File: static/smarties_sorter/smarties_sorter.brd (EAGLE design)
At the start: 170.2 x 100 mm, 18 parts, among them IC1 MEGA8-P, Q1 16Mhz, Q2 IRLZ44Z

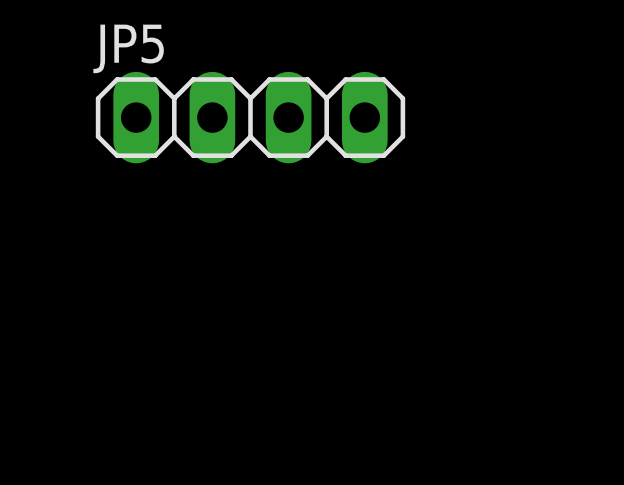
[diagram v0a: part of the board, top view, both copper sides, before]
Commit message: [smarties_sorter] Adds capa on the motor
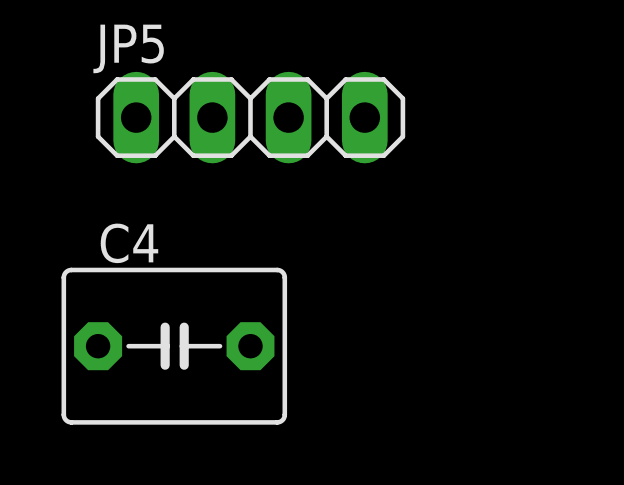
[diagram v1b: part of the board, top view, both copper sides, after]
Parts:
- added C4: 10µF, capacitor-wima:C5B5
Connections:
- net 5V: now also C4.2
- net N$7: now also C4.1
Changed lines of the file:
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@@
 <element name="R1" library="rcl" package="0414/15" value="10Kohms" x="8.89" y="-5.08"/>
 <element name="JP5" library="pinhead" package="1X04" value="" x="6.35" y="-11.43"/>
+<element name="C4" library="capacitor-wima" package="C5B5" value="10µF" x="3.81" y="-19.05"/>
 </elements>
 <signals>
@@
 <wire x1="57.15" y1="67.31" x2="60.96" y2="67.31" width="0.8128" layer="16"/>
 <contactref element="JP5" pad="1"/>
+<contactref element="C4" pad="2"/>
 <wire x1="110.49" y1="67.31" x2="102.87" y2="67.31" width="0" layer="19" extent="16-16"/>
 <wire x1="2.54" y1="-11.43" x2="52.07" y2="31.75" width="0" layer="19" extent="16-16"/>
+<wire x1="6.35" y1="-19.05" x2="2.54" y2="-11.43" width="0" layer="19" extent="1-1"/>
 </signal>
 <signal name="N$6">
@@
 <wire x1="49.53" y1="64.77" x2="48.26" y2="64.77" width="0.8128" layer="16"/>
 <contactref element="D2" pad="A"/>
+<contactref element="C4" pad="1"/>
+<wire x1="1.27" y1="-19.05" x2="48.26" y2="64.77" width="0" layer="19" extent="1-1"/>
 </signal>
 <signal name="N$9">

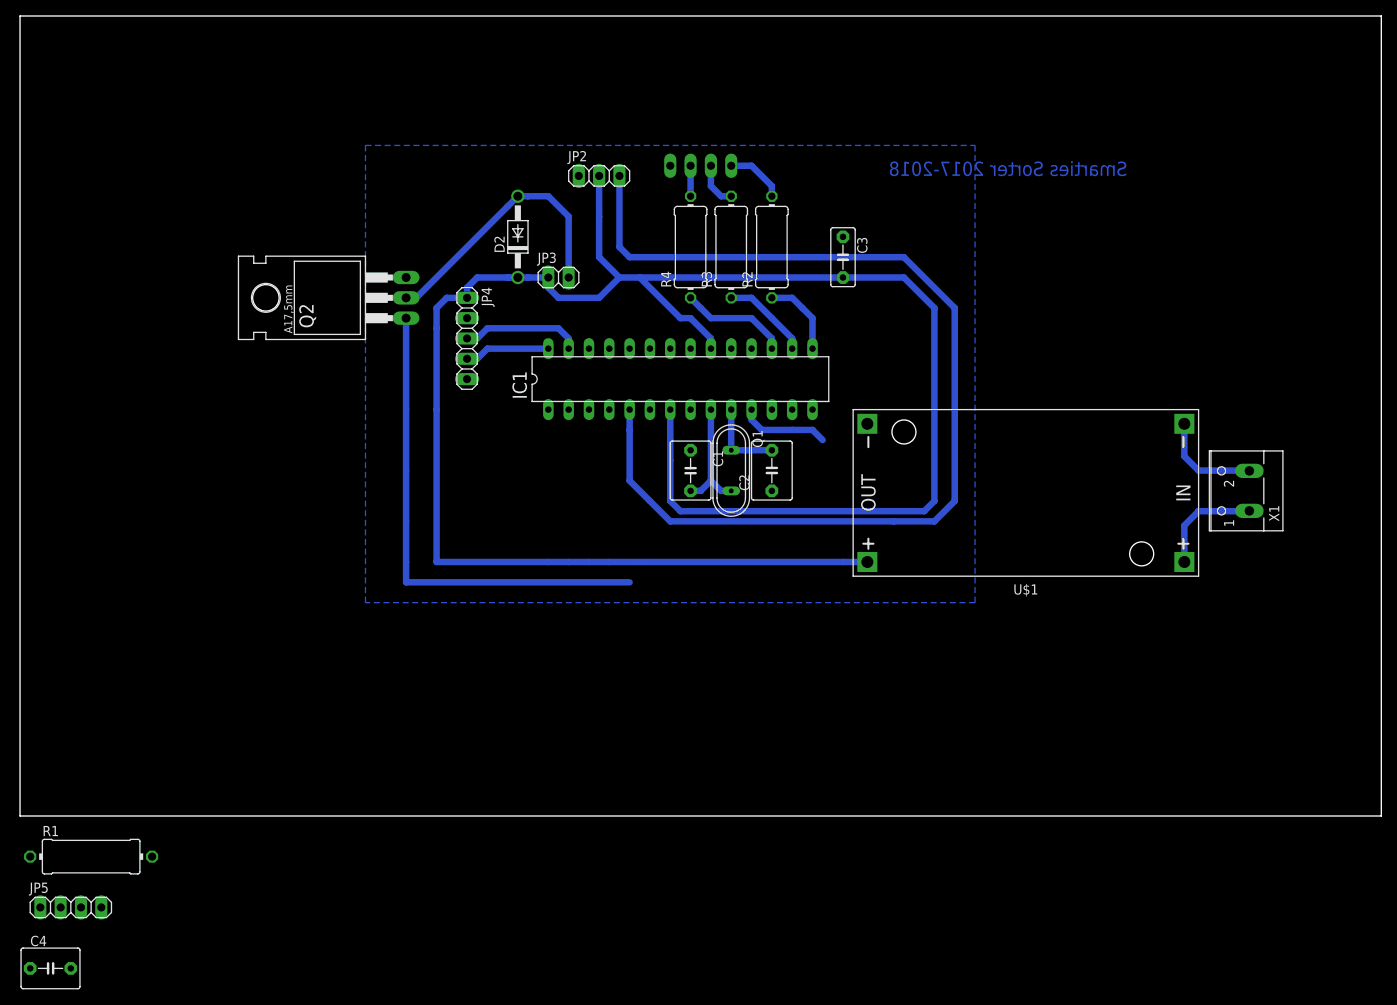
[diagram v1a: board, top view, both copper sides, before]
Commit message: [smarties_sorter] Change buck to ls7805 and route everything.
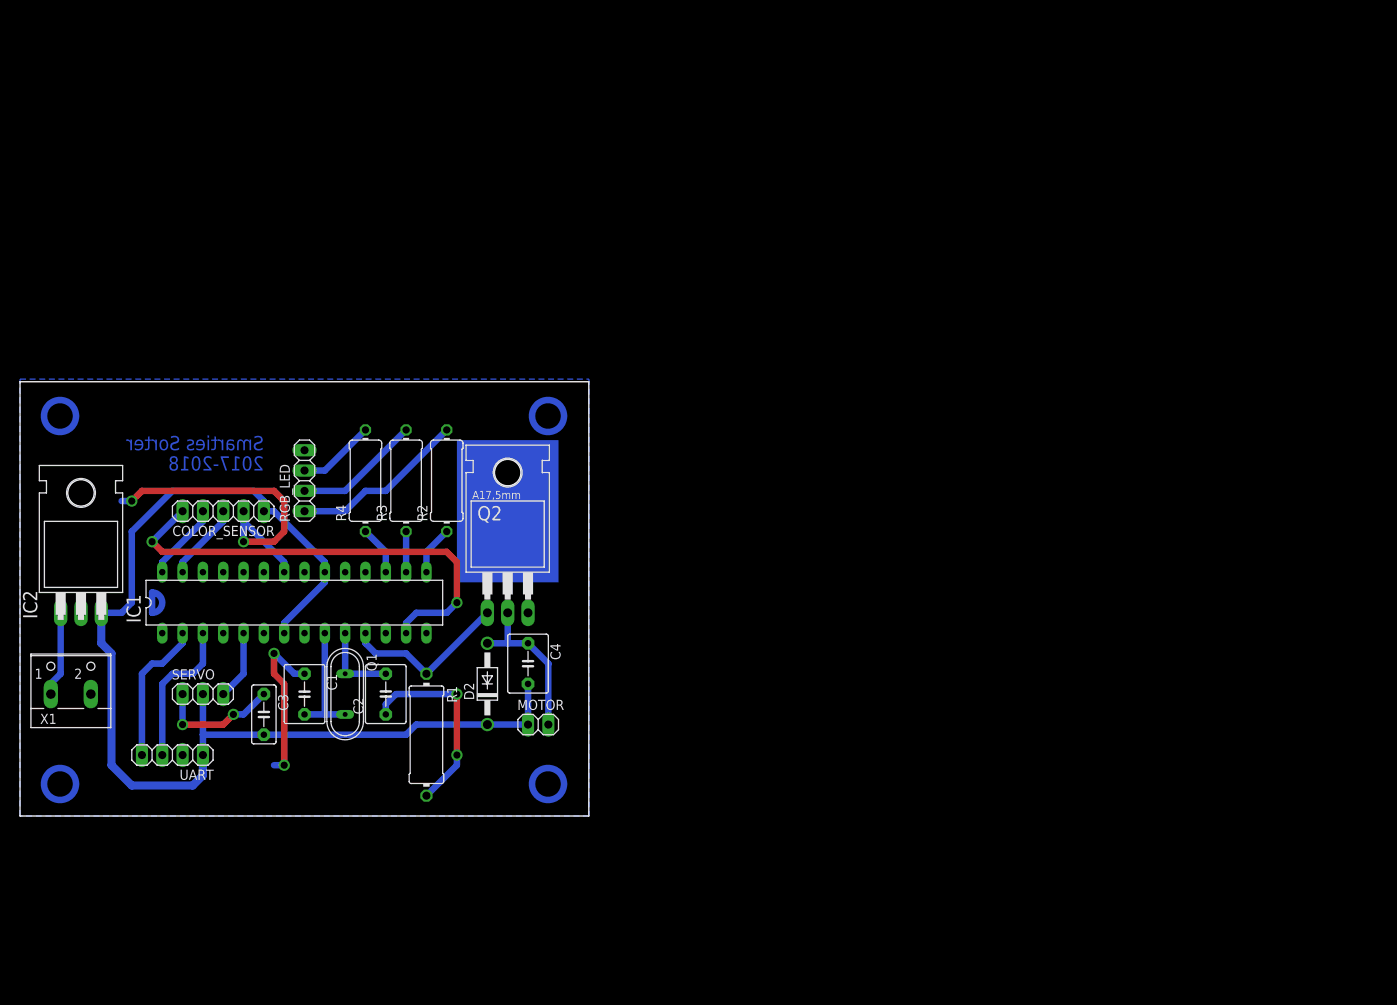
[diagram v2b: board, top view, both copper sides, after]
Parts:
- removed JP1, JP5: (no value), pinhead:1X04
- removed JP2: (no value), pinhead:1X03
- removed JP3: (no value), pinhead:1X02
- removed JP4: (no value), pinhead:1X05
- removed U$1: DC-DC-STEP-DOWN-LM2596, diy-modules:DC-DC-STEP-DOWN-LM2596
- added COLOR_SENSOR: (no value), pinhead:1X05
- added IC2: 7805T, linear:TO220H
- added MOTOR: (no value), pinhead:1X02
- added RGB_LED, UART: (no value), pinhead:1X04
- added SERVO: (no value), pinhead:1X03
- moved X1 148.0 mm to (6.35, 16.5), turned to 0 degrees
- moved C3 92.2 mm to (30.5, 12.7)
- moved C4 70.8 mm to (63.5, 19.1), turned to 270 degrees
- moved D2 56.0 mm to (58.4, 16.5)
- moved C2 55.8 mm to (45.7, 15.2)
- moved IC1 55.8 mm to (34.3, 26.7)
- moved Q1 55.8 mm to (40.6, 15.2)
- moved C1 55.8 mm to (35.6, 15.2)
- moved R2 50.0 mm to (53.3, 41.9)
- moved R3 50.0 mm to (48.3, 41.9)
- moved R4 50.0 mm to (43.2, 41.9)
- moved R1 44.6 mm to (50.8, 10.2), turned to 270 degrees
- moved Q2 38.1 mm to (61.0, 31.8), turned to 0 degrees
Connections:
- net N$11 renamed B_LED
- net N$3 renamed G_LED
- net N$4 renamed R_LED
- net N$9 renamed MOTOR_CMD
- removed net 12V_GND: U$1.IN-, X1.2
- removed net N$13: IC1.2, JP5.4
- removed net N$16: IC1.28, JP4.4
- removed net N$17: IC1.27, JP4.3
- removed net N$6: IC1.5, JP2.3
- removed net N$7: C4.1, D2.A, JP3.2, Q2.D
- removed net N$8: IC1.3, JP5.3
- new net DRAIN: C4.1, D2.A, MOTOR.2, Q2.D
- new net RX: IC1.2, UART.4
- new net SCL: COLOR_SENSOR.4, IC1.28
- new net SDA: COLOR_SENSOR.3, IC1.27
- new net SERVO_CMD: IC1.5, SERVO.3
- new net TX: IC1.3, UART.3
- net 12V: now also IC2.1; no longer U$1.IN+
- net 5V: now also COLOR_SENSOR.1, IC2.3, MOTOR.1, SERVO.2, UART.1; no longer JP2.2, JP3.1, JP4.1, JP5.1, U$1.OUT+
- net GND: now also COLOR_SENSOR.2, IC2.2, RGB_LED.4, SERVO.1, UART.2, X1.2; no longer JP1.4, JP2.1, JP4.2, JP5.2, U$1.OUT-
- net LED_CTRL: now also COLOR_SENSOR.5; no longer JP4.5
- net N$10: now also RGB_LED.2; no longer JP1.2
- net N$12: now also RGB_LED.3; no longer JP1.3
- net N$5: now also RGB_LED.1; no longer JP1.1
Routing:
- net N$6: track 130.8 -> 0.00 mm
- net 5V: track 252.5 -> 143.9 mm
- net GND: track 1.27 -> 105.5 mm, vias 0 -> 8
- net LED_CTRL: track 0.00 -> 58.3 mm, vias 0 -> 2
- net MOTOR_CMD: track 72.2 -> 21.2 mm
- net N$7: track 34.3 -> 0.00 mm
- net DRAIN: track 0.00 -> 20.1 mm
- net TX: track 0.00 -> 18.8 mm
- net RX: track 0.00 -> 18.1 mm
- net N$17: track 15.0 -> 0.00 mm
- net N$5: track 7.40 -> 22.0 mm
- net 12V_GND: track 12.9 -> 0.00 mm
- net N$16: track 10.7 -> 0.00 mm
- net N$10: track 5.61 -> 15.9 mm
- net SDA: track 0.00 -> 9.72 mm
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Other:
- board size 170.2 x 100 mm -> 71.1 x 54.3 mm
- board text added: "2017-2018"
- board text added: "Smarties Sorter"
- board text removed: "Smarties Sorter 2017-2018"
